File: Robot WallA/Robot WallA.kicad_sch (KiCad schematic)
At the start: 4 parts

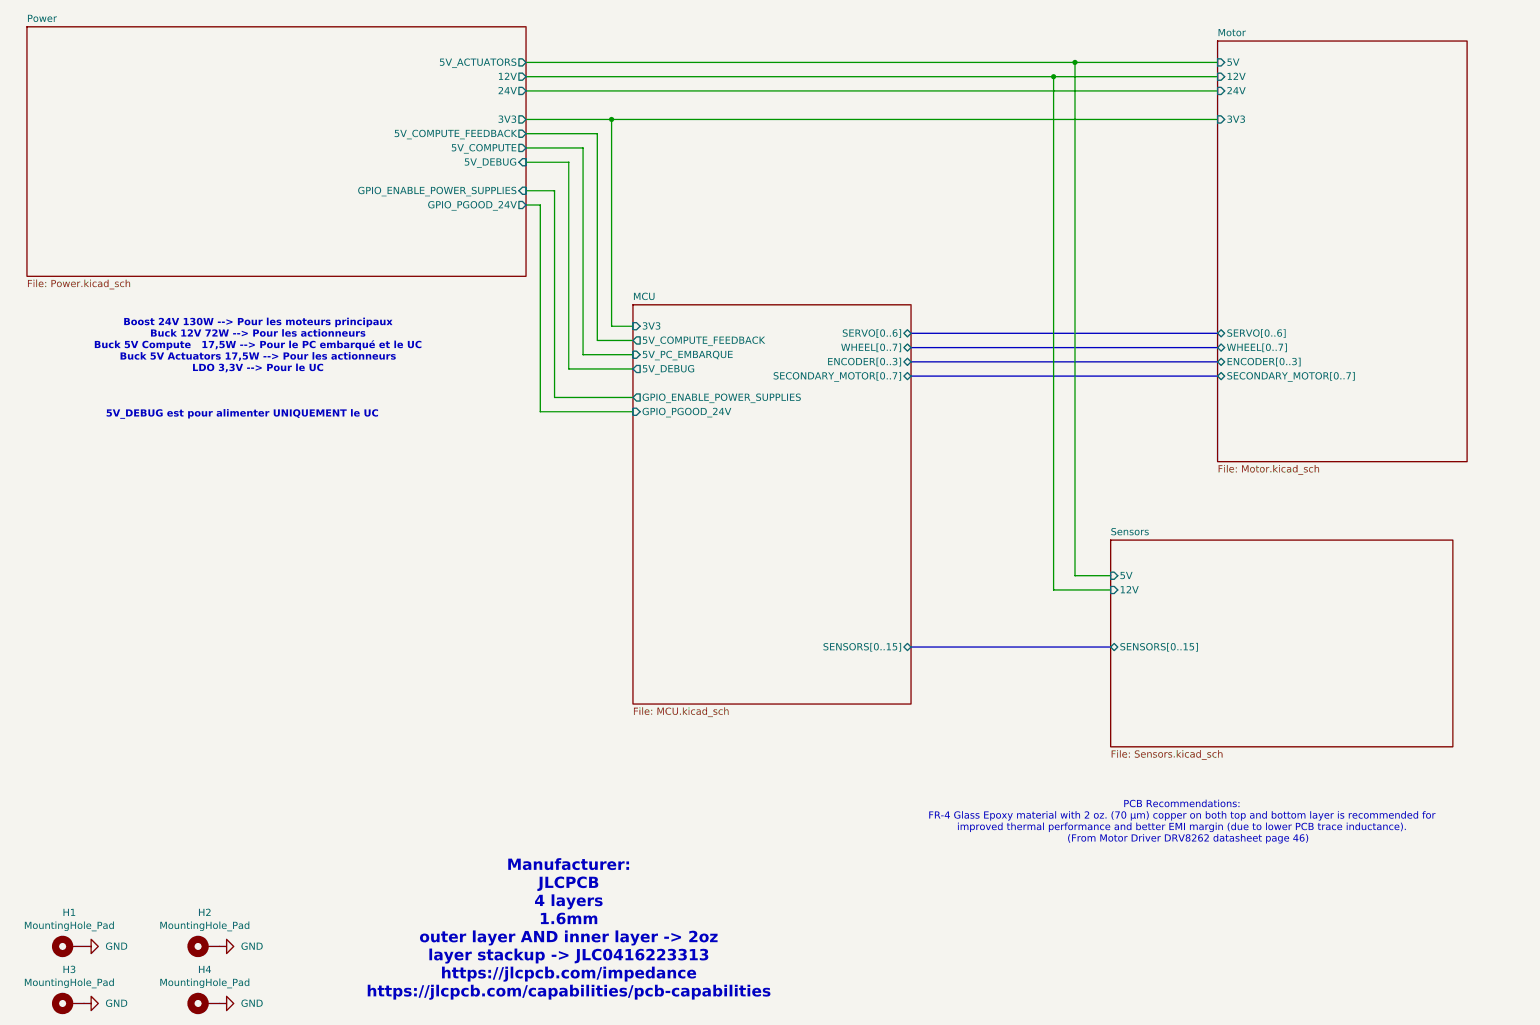
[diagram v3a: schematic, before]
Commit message: Added 3 thermistor to measure temperature near 12V and 24V power supplies and near motor drivers
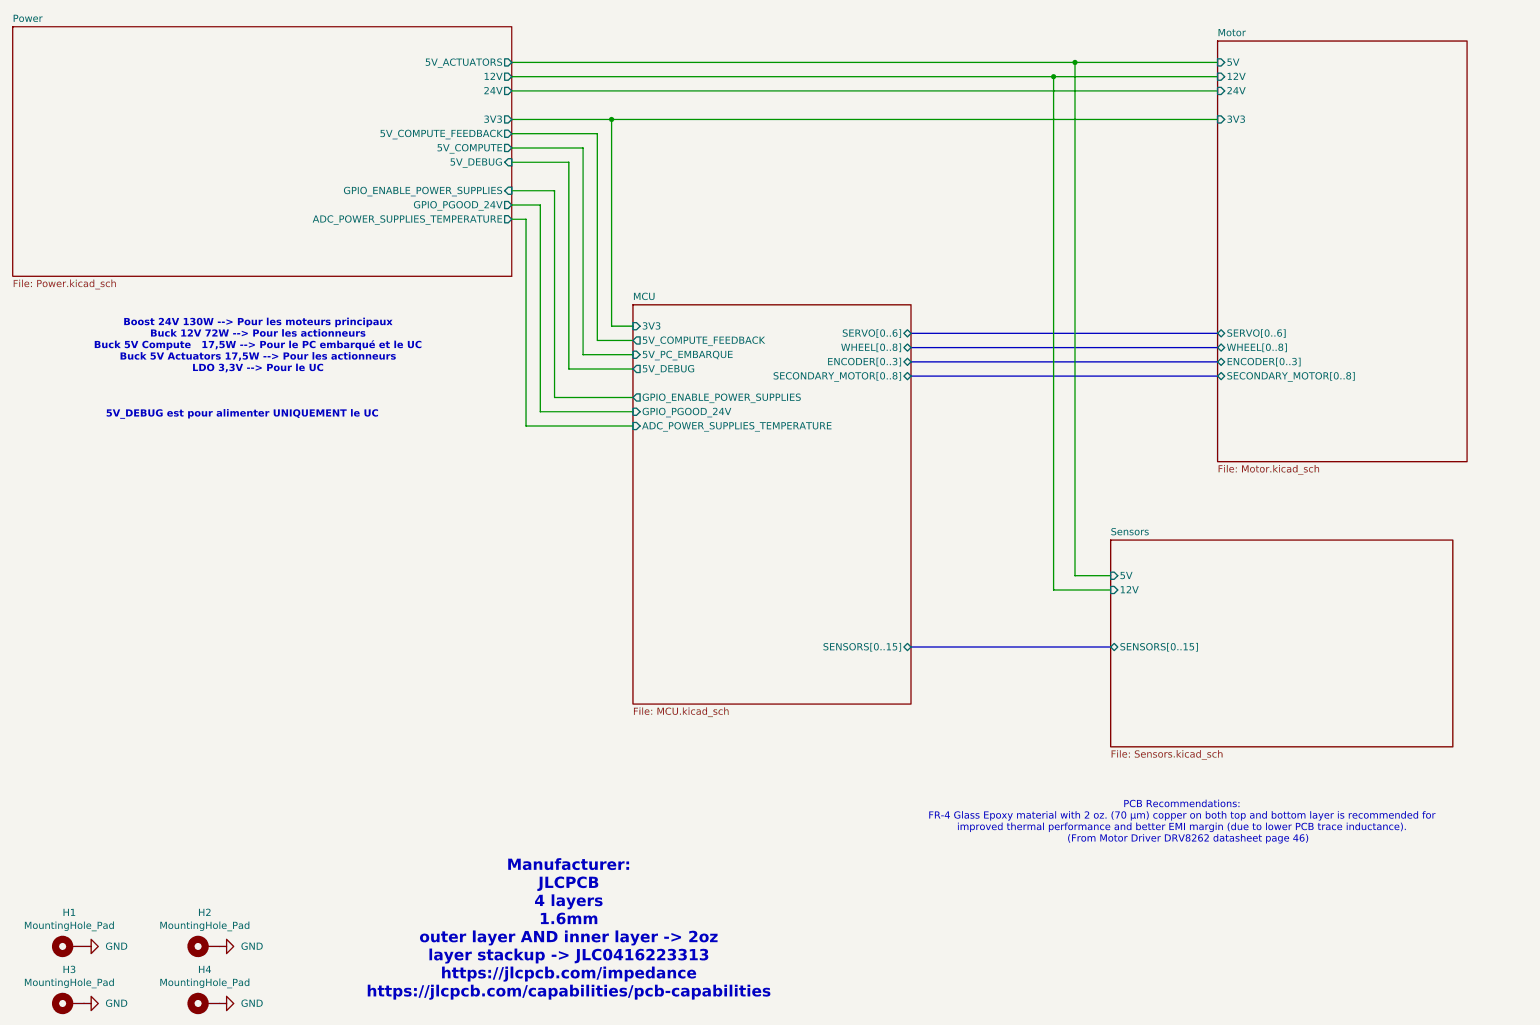
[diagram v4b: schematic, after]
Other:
- sheet MCU ports: added ADC_POWER_SUPPLIES_TEMPERATURE, SECONDARY_MOTOR[0..8], WHEEL[0..8]; removed SECONDARY_MOTOR[0..7], WHEEL[0..7]
- sheet Motor ports: added SECONDARY_MOTOR[0..8], WHEEL[0..8]; removed SECONDARY_MOTOR[0..7], WHEEL[0..7]
- sheet Power ports: added ADC_POWER_SUPPLIES_TEMPERATURE; removed none
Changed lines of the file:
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@@
 	(wire
 		(pts
-			(xy 109.22 25.4) (xy 203.2 25.4)
+			(xy 106.68 50.8) (xy 109.22 50.8)
+		)
+		(stroke
+			(width 0)
+			(type default)
+		)
+	)
+	(wire
+		(pts
+			(xy 109.22 87.63) (xy 128.27 87.63)
+		)
+		(stroke
+			(width 0)
+			(type default)
+		)
+	)
+	(wire
+		(pts
+			(xy 106.68 25.4) (xy 203.2 25.4)
 		)
 		(stroke
@@
 	(wire
 		(pts
-			(xy 109.22 27.94) (xy 232.41 27.94)
+			(xy 106.68 27.94) (xy 232.41 27.94)
 		)
 		(stroke
@@
 	(wire
 		(pts
-			(xy 109.22 33.02) (xy 124.46 33.02)
-		)
-		(stroke
-			(width 0)
-			(type default)
-		)
-	)
-	(wire
-		(pts
-			(xy 109.22 48.26) (xy 111.76 48.26)
+			(xy 106.68 33.02) (xy 124.46 33.02)
+		)
+		(stroke
+			(width 0)
+			(type default)
+		)
+	)
+	(wire
+		(pts
+			(xy 106.68 48.26) (xy 111.76 48.26)
 		)
 		(stroke
@@
 	(wire
 		(pts
+			(xy 109.22 50.8) (xy 109.22 87.63)
+		)
+		(stroke
+			(width 0)
+			(type default)
+		)
+	)
+	(wire
+		(pts
 			(xy 203.2 116.84) (xy 203.2 25.4)
 		)
@@
 	(wire
 		(pts
-			(xy 109.22 35.56) (xy 121.92 35.56)
+			(xy 106.68 35.56) (xy 121.92 35.56)
 		)
 		(stroke
@@
 	(wire
 		(pts
-			(xy 109.22 38.1) (xy 119.38 38.1)
-		)
-		(stroke
-			(width 0)
-			(type default)
-		)
-	)
-	(wire
-		(pts
-			(xy 116.84 40.64) (xy 109.22 40.64)
+			(xy 106.68 38.1) (xy 119.38 38.1)
+		)
+		(stroke
+			(width 0)
+			(type default)
+		)
+	)
+	(wire
+		(pts
+			(xy 116.84 40.64) (xy 106.68 40.64)
 		)
 		(stroke
@@
 	(wire
 		(pts
-			(xy 109.22 22.86) (xy 207.01 22.86)
-		)
-		(stroke
-			(width 0)
-			(type default)
-		)
-	)
-	(wire
-		(pts
-			(xy 114.3 45.72) (xy 109.22 45.72)
+			(xy 106.68 22.86) (xy 207.01 22.86)
+		)
+		(stroke
+			(width 0)
+			(type default)
+		)
+	)
+	(wire
+		(pts
+			(xy 114.3 45.72) (xy 106.68 45.72)
 		)
 		(stroke
@@
 			)
 		)
-		(pin "WHEEL[0..7]" bidirectional
+		(pin "WHEEL[0..8]" bidirectional
 			(at 232.41 73.66 180)
 			(effects
@@
 			)
 		)
-		(pin "SECONDARY_MOTOR[0..7]" bidirectional
+		(pin "SECONDARY_MOTOR[0..8]" bidirectional
 			(at 232.41 78.74 180)
 			(effects
@@
 			)
 		)
-		(pin "WHEEL[0..7]" bidirectional
+		(pin "WHEEL[0..8]" bidirectional
 			(at 177.8 73.66 0)
 			(effects
@@
 			)
 		)
-		(pin "SECONDARY_MOTOR[0..7]" bidirectional
+		(pin "SECONDARY_MOTOR[0..8]" bidirectional
 			(at 177.8 78.74 0)
 			(effects
@@
 		(pin "5V_COMPUTE_FEEDBACK" output
 			(at 128.27 72.39 180)
+			(effects
+				(font
+					(size 1.27 1.27)
+				)
+				(justify left)
+			)
+		)
+		(pin "ADC_POWER_SUPPLIES_TEMPERATURE" input
+			(at 128.27 87.63 180)
 			(effects
 				(font
@@
 	)
 	(sheet
-		(at 20.32 16.51)
+		(at 17.78 16.51)
 		(size 88.9 44.45)
 		(exclude_from_sim no)
@@
 		)
 		(property "Sheetname" "Power"
-			(at 20.32 15.7984 0)
+			(at 17.78 15.7984 0)
 			(effects
 				(font
@@
 		)
 		(property "Sheetfile" "Power.kicad_sch"
-			(at 20.32 61.5446 0)
+			(at 17.78 61.5446 0)
 			(effects
 				(font
@@
 		)
 		(pin "3V3" output
-			(at 109.22 33.02 0)
+			(at 106.68 33.02 0)
 			(effects
 				(font
@@
 		)
 		(pin "24V" output
-			(at 109.22 27.94 0)
+			(at 106.68 27.94 0)
 			(effects
 				(font
@@
 		)
 		(pin "GPIO_PGOOD_24V" output
-			(at 109.22 48.26 0)
+			(at 106.68 48.26 0)
 			(effects
 				(font
@@
 		)
 		(pin "5V_DEBUG" input
-			(at 109.22 40.64 0)
+			(at 106.68 40.64 0)
 			(effects
 				(font
@@
 		)
 		(pin "12V" output
-			(at 109.22 25.4 0)
+			(at 106.68 25.4 0)
 			(effects
 				(font
@@
 		)
 		(pin "5V_ACTUATORS" output
-			(at 109.22 22.86 0)
+			(at 106.68 22.86 0)
 			(effects
 				(font
@@
 		)
 		(pin "5V_COMPUTE" output
-			(at 109.22 38.1 0)
+			(at 106.68 38.1 0)
 			(effects
 				(font
@@
 		)
 		(pin "GPIO_ENABLE_POWER_SUPPLIES" input
-			(at 109.22 45.72 0)
+			(at 106.68 45.72 0)
 			(effects
 				(font
@@
 		)
 		(pin "5V_COMPUTE_FEEDBACK" output
-			(at 109.22 35.56 0)
-			(effects
-				(font
+			(at 106.68 35.56 0)
+			(effects
+				(font
+					(size 1.27 1.27)
+				)
+				(justify right)
+			)
+		)
+		(pin "ADC_POWER_SUPPLIES_TEMPERATURE" output
+			(at 106.68 50.8 0)
+			(effects
+				(font

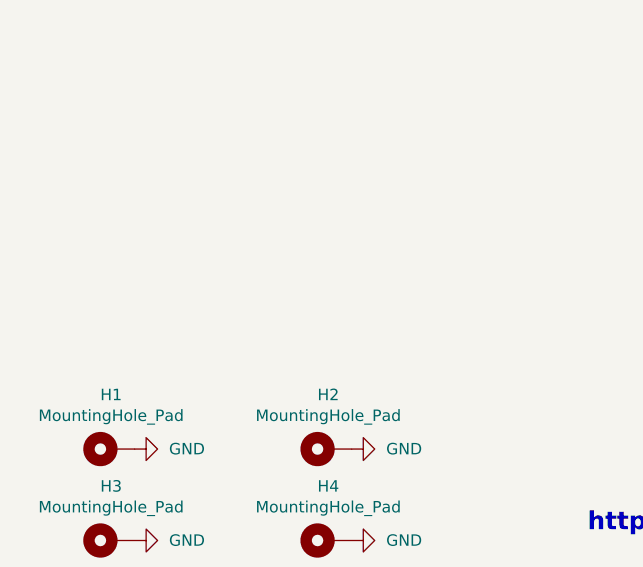
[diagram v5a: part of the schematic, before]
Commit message: Added logo
Replaced out of stock components
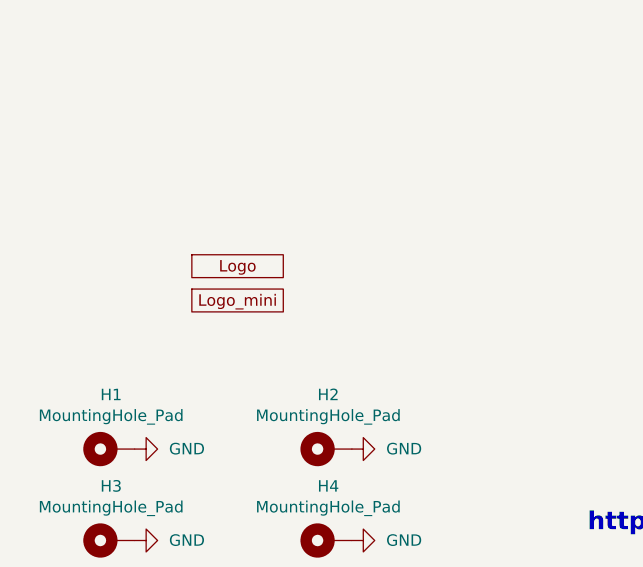
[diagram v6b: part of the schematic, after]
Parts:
- added U11: ~, Library:Logo_Wall-A, symbol Library:Logo
- added U12: ~, Library:Logo_mini_Wall-A, symbol Library:Logo_mini
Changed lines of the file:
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@@
+	)
+	(symbol
+		(lib_id "Library:Logo")
+		(at 41.91 160.02 0)
+		(unit 1)
+		(exclude_from_sim no)
+		(in_bom yes)
+		(on_board yes)
+		(dnp no)
+		(fields_autoplaced yes)
+		(property "Reference" "U11"
+			(at 41.91 157.734 0)
+			(effects
+				(font
+					(size 1.27 1.27)
+				)
+				(hide yes)
+			)
+		)
+		(property "Value" "~"
+			(at 41.91 156.21 0)
+			(effects
+				(font
+					(size 1.27 1.27)
+				)
+				(hide yes)
+			)
+		)
+		(property "Footprint" "Library:Logo_Wall-A"
+			(at 41.656 155.448 0)
+			(effects
+				(font
+					(size 1.27 1.27)
+				)
+				(hide yes)
+			)
+		)
+		(property "Datasheet" ""
+			(at 41.91 160.02 0)
+			(effects
+				(font
+					(size 1.27 1.27)
+				)
+				(hide yes)
+			)
+		)
+		(property "Description" ""
+			(at 41.91 160.02 0)
+			(effects
+				(font
+					(size 1.27 1.27)
+				)
+				(hide yes)
+			)
+		)
+		(instances
+			(project ""
+				(path "/117fd49e-499d-4b54-b58c-f6b538ecca4a"
+					(reference "U11")
+					(unit 1)
+				)
+			)
+		)
+	)
+	(symbol
+		(lib_id "Library:Logo_mini")
+		(at 41.91 163.83 0)
+		(unit 1)
+		(exclude_from_sim no)
+		(in_bom yes)
+		(on_board yes)
+		(dnp no)
+		(fields_autoplaced yes)
+		(property "Reference" "U12"
+			(at 41.91 161.544 0)
+			(effects
+				(font
+					(size 1.27 1.27)
+				)
+				(hide yes)
+			)
+		)
+		(property "Value" "~"
+			(at 41.91 160.02 0)
+			(effects
+				(font
+					(size 1.27 1.27)
+				)
+				(hide yes)
+			)
+		)
+		(property "Footprint" "Library:Logo_mini_Wall-A"
+			(at 41.656 159.258 0)
+			(effects
+				(font
+					(size 1.27 1.27)
+				)
+				(hide yes)
+			)
+		)
+		(property "Datasheet" ""
+			(at 41.91 163.83 0)
+			(effects
+				(font
+					(size 1.27 1.27)
+				)
+				(hide yes)
+			)
+		)
+		(property "Description" ""
+			(at 41.91 163.83 0)
+			(effects
+				(font
+					(size 1.27 1.27)
+				)
+				(hide yes)
+			)
+		)
+		(instances
+			(project ""
+				(path "/117fd49e-499d-4b54-b58c-f6b538ecca4a"
+					(reference "U12")
+					(unit 1)
+				)
+			)
+		)
 	)
 	(symbol
